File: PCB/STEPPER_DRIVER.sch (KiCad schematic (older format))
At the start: 7 parts, among them J3 Screw_Terminal_01x04, J4 Conn_01x04_Female

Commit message: Added Dielectric and voltage rating to all capacitors
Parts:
- C10, C9: Dielectric (none) -> X7R
- C11: Dielectric (none) -> Tantalum
- C12: Dielectric (none) -> Aluminium Film; Impedance (none) -> General Purpose; Lifetime @ Temperature (none) -> 1000hr @ 85degC
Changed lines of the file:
@@
 $Descr A4 11693 8268
 encoding utf-8
-Sheet 3 20
+Sheet 13 20
 Title ""
 Date ""
@@
 F 3 "" H 5950 2500 50  0001 C CNN
 F 4 "50V" H 5950 2500 50  0001 C CNN "Voltage Rating"
+F 5 "Tantalum" H 5950 2500 50  0001 C CNN "Dielectric"
 	1    5950 2500
 	1    0    0    -1
@@
 F 3 "" H 5600 2500 50  0001 C CNN
 F 4 "50V" H 5600 2500 50  0001 C CNN "Voltage Rating"
+F 5 "X7R" H 5600 2500 50  0001 C CNN "Dielectric"
 	1    5600 2500
 	1    0    0    -1
@@
 F 3 "" H 6350 2500 50  0001 C CNN
 F 4 "50V" H 6350 2500 50  0001 C CNN "Voltage Rating"
+F 5 "Aluminium Film" H 6350 2500 50  0001 C CNN "Dielectric"
+F 6 "General Purpose" H 6350 2500 50  0001 C CNN "Impedance"
+F 7 "1000hr @ 85degC" H 6350 2500 50  0001 C CNN "Lifetime @ Temperature"
 	1    6350 2500
 	1    0    0    -1
@@
 F 3 "" H 5250 2500 50  0001 C CNN
 F 4 "6.3V" H 5250 2500 50  0001 C CNN "Voltage Rating"
+F 5 "X7R" H 5250 2500 50  0001 C CNN "Dielectric"
 	1    5250 2500
 	1    0    0    -1

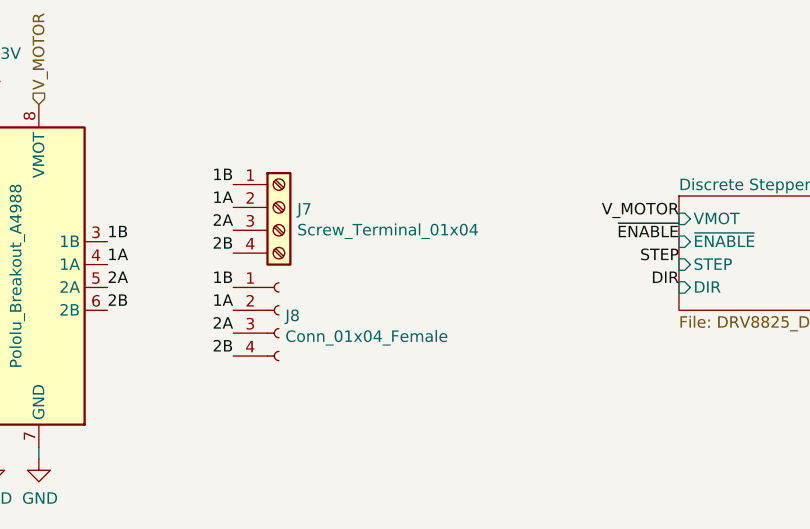
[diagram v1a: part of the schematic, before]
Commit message: Named elements with missing values
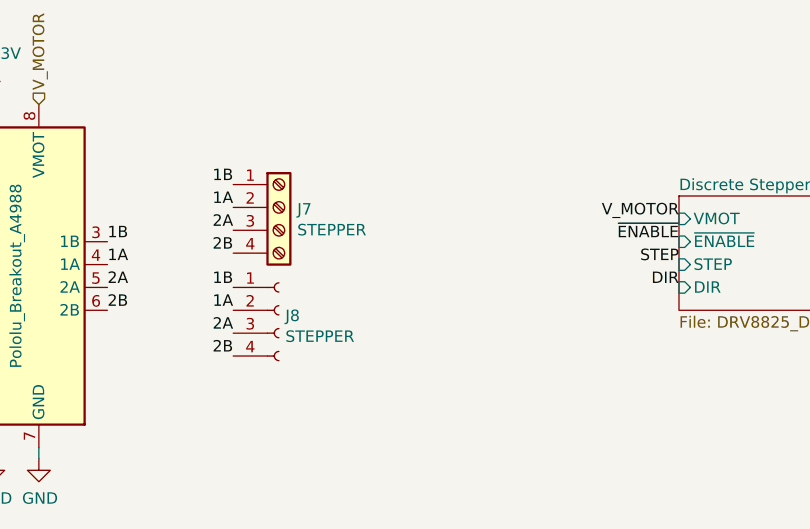
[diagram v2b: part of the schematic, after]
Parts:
- J3: value Screw_Terminal_01x04 -> STEPPER
- J4: value Conn_01x04_Female -> STEPPER
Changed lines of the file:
@@
 $Descr A4 11693 8268
 encoding utf-8
-Sheet 13 20
+Sheet 3 20
 Title ""
 Date ""
@@
 AR Path="/5E8813FF/5E8A7820" Ref="J8"  Part="1"
 F 0 "J8" H 6978 4226 50  0000 L CNN
-F 1 "Conn_01x04_Female" H 6978 4135 50  0000 L CNN
+F 1 "STEPPER" H 6978 4135 50  0000 L CNN
 F 2 "" H 6950 4250 50  0001 C CNN
 F 3 "" H 6950 4250 50  0001 C CNN
@@
 AR Path="/5E8813FF/5E8A82D9" Ref="J7"  Part="1"
 F 0 "J7" H 7030 3792 50  0000 L CNN
-F 1 "Screw_Terminal_01x04" H 7030 3701 50  0000 L CNN
+F 1 "STEPPER" H 7030 3701 50  0000 L CNN
 F 2 "" H 6950 3800 50  0001 C CNN
 F 3 "" H 6950 3800 50  0001 C CNN
@@
 AR Path="/5E8A6686/5E8421AB" Ref="#PWR033"  Part="1"
 AR Path="/5E8813FF/5E8421AB" Ref="#PWR096"  Part="1"
-F 0 "#PWR096" H 5700 3150 50  0001 C CNN
+F 0 "#PWR033" H 5700 3150 50  0001 C CNN
 F 1 "+3.3V" H 5715 3473 50  0000 C CNN
 F 2 "" H 5700 3300 50  0001 C CNN
@@
 AR Path="/5E8A6686/5E842853" Ref="#PWR034"  Part="1"
 AR Path="/5E8813FF/5E842853" Ref="#PWR097"  Part="1"
-F 0 "#PWR097" H 5700 4650 50  0001 C CNN
+F 0 "#PWR034" H 5700 4650 50  0001 C CNN
 F 1 "GND" H 5705 4727 50  0000 C CNN
 F 2 "" H 5700 4900 50  0001 C CNN
@@
 AR Path="/5E8A6686/5E842AD6" Ref="#PWR035"  Part="1"
 AR Path="/5E8813FF/5E842AD6" Ref="#PWR098"  Part="1"
-F 0 "#PWR098" H 5900 4650 50  0001 C CNN
+F 0 "#PWR035" H 5900 4650 50  0001 C CNN
 F 1 "GND" H 5905 4727 50  0000 C CNN
 F 2 "" H 5900 4900 50  0001 C CNN
@@
 AR Path="/5E8A6686/5E84D212" Ref="#PWR027"  Part="1"
 AR Path="/5E8813FF/5E84D212" Ref="#PWR090"  Part="1"
-F 0 "#PWR090" H 5250 3400 50  0001 C CNN
+F 0 "#PWR027" H 5250 3400 50  0001 C CNN
 F 1 "GND" V 5255 3522 50  0000 R CNN
 F 2 "" H 5250 3650 50  0001 C CNN
@@
 AR Path="/5E8A6686/5E8548E7" Ref="#PWR036"  Part="1"
 AR Path="/5E8813FF/5E8548E7" Ref="#PWR099"  Part="1"
-F 0 "#PWR099" H 5950 2400 50  0001 C CNN
+F 0 "#PWR036" H 5950 2400 50  0001 C CNN
 F 1 "GND" H 5955 2477 50  0000 C CNN
 F 2 "" H 5950 2650 50  0001 C CNN
@@
 AR Path="/5E8A6686/5E8572FE" Ref="#PWR032"  Part="1"
 AR Path="/5E8813FF/5E8572FE" Ref="#PWR095"  Part="1"
-F 0 "#PWR095" H 5600 2400 50  0001 C CNN
+F 0 "#PWR032" H 5600 2400 50  0001 C CNN
 F 1 "GND" H 5605 2477 50  0000 C CNN
 F 2 "" H 5600 2650 50  0001 C CNN
@@
 AR Path="/5E8A6686/5E85775C" Ref="#PWR037"  Part="1"
 AR Path="/5E8813FF/5E85775C" Ref="#PWR0100"  Part="1"
-F 0 "#PWR0100" H 6350 2400 50  0001 C CNN
+F 0 "#PWR037" H 6350 2400 50  0001 C CNN
 F 1 "GND" H 6355 2477 50  0000 C CNN
 F 2 "" H 6350 2650 50  0001 C CNN
@@
 AR Path="/5E8A6686/5E860428" Ref="#PWR026"  Part="1"
 AR Path="/5E8813FF/5E860428" Ref="#PWR089"  Part="1"
-F 0 "#PWR089" H 5250 2400 50  0001 C CNN
+F 0 "#PWR026" H 5250 2400 50  0001 C CNN
 F 1 "GND" H 5255 2477 50  0000 C CNN
 F 2 "" H 5250 2650 50  0001 C CNN
@@
 AR Path="/5E8A6686/5E8608E5" Ref="#PWR025"  Part="1"
 AR Path="/5E8813FF/5E8608E5" Ref="#PWR088"  Part="1"
-F 0 "#PWR088" H 5250 2200 50  0001 C CNN
+F 0 "#PWR025" H 5250 2200 50  0001 C CNN
 F 1 "+3.3V" H 5265 2523 50  0000 C CNN
 F 2 "" H 5250 2350 50  0001 C CNN
@@
 AR Path="/5E8A6686/5E8CF9B2" Ref="#PWR028"  Part="1"
 AR Path="/5E8813FF/5E8CF9B2" Ref="#PWR091"  Part="1"
-F 0 "#PWR091" H 5250 3500 50  0001 C CNN
+F 0 "#PWR028" H 5250 3500 50  0001 C CNN
 F 1 "GND" V 5255 3622 50  0000 R CNN
 F 2 "" H 5250 3750 50  0001 C CNN
@@
 AR Path="/5E8A6686/5E8FF25B" Ref="#PWR029"  Part="1"
 AR Path="/5E8813FF/5E8FF25B" Ref="#PWR092"  Part="1"
-F 0 "#PWR092" H 5250 4100 50  0001 C CNN
+F 0 "#PWR029" H 5250 4100 50  0001 C CNN
 F 1 "GND" V 5255 4222 50  0000 R CNN
 F 2 "" H 5250 4350 50  0001 C CNN
@@
 AR Path="/5E8A6686/5E8FF51C" Ref="#PWR030"  Part="1"
 AR Path="/5E8813FF/5E8FF51C" Ref="#PWR093"  Part="1"
-F 0 "#PWR093" H 5250 4200 50  0001 C CNN
+F 0 "#PWR030" H 5250 4200 50  0001 C CNN
 F 1 "GND" V 5255 4322 50  0000 R CNN
 F 2 "" H 5250 4450 50  0001 C CNN
@@
 AR Path="/5E8A6686/5E8FF61C" Ref="#PWR031"  Part="1"
 AR Path="/5E8813FF/5E8FF61C" Ref="#PWR094"  Part="1"
-F 0 "#PWR094" H 5250 4300 50  0001 C CNN
+F 0 "#PWR031" H 5250 4300 50  0001 C CNN
 F 1 "GND" V 5255 4422 50  0000 R CNN
 F 2 "" H 5250 4550 50  0001 C CNN

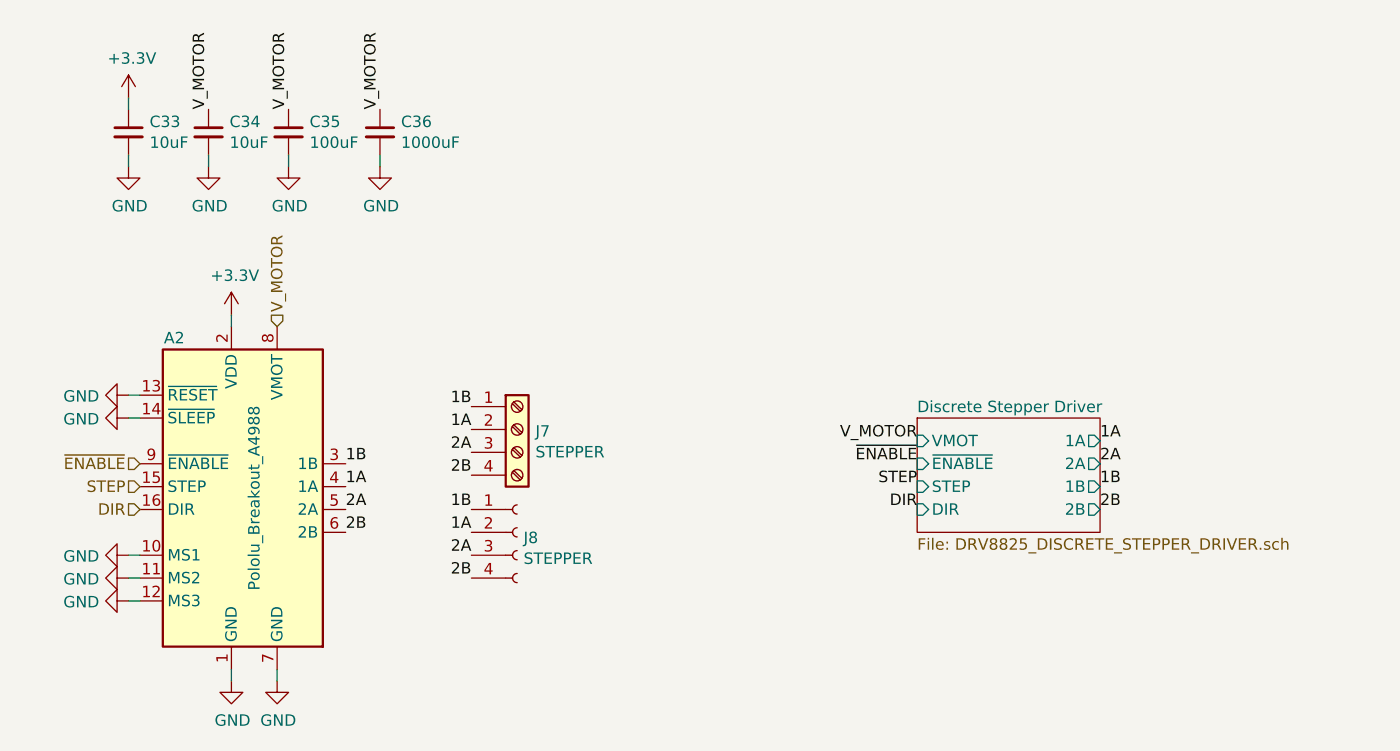
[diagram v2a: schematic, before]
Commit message: Added some footprints
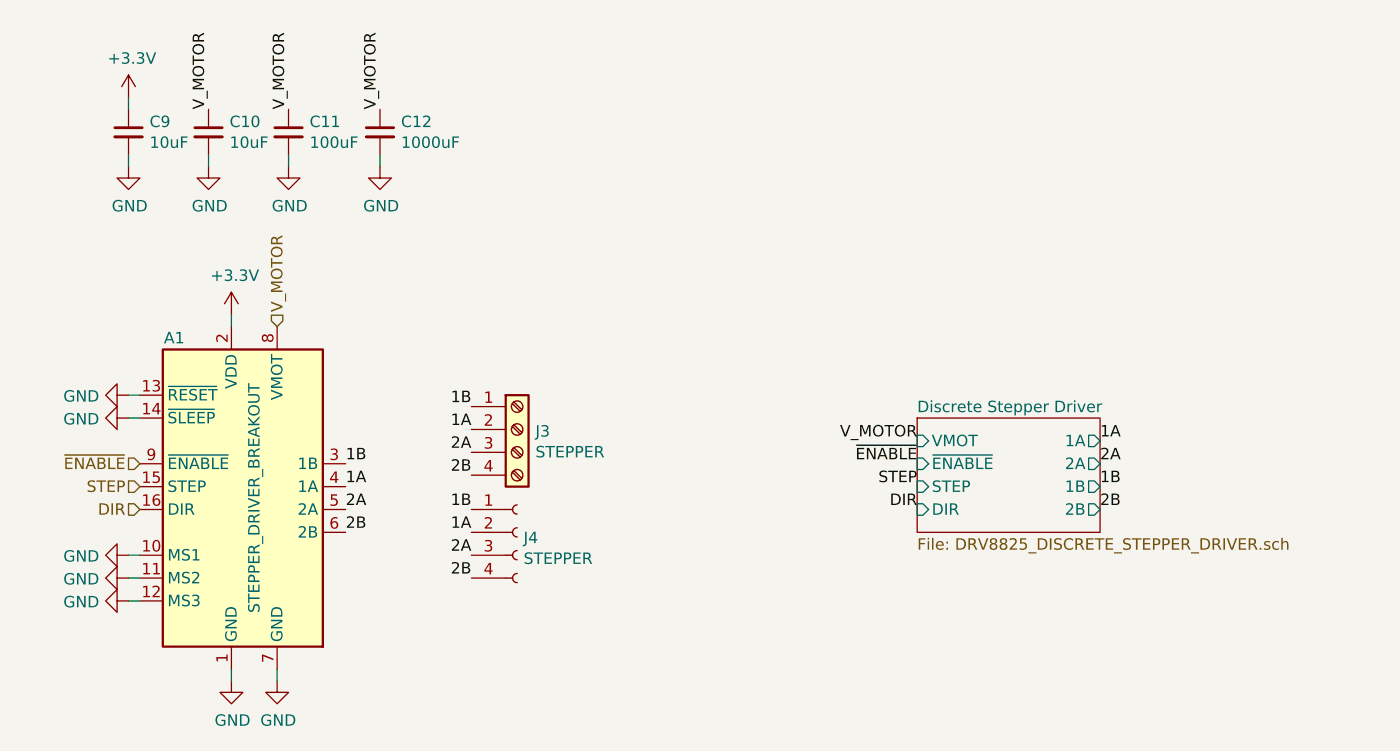
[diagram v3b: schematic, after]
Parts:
- A1: value Pololu_Breakout_A4988 -> STEPPER_DRIVER_BREAKOUT
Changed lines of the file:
@@
 AR Path="/5E8A6686/5E8A6F90" Ref="A1"  Part="1"
 AR Path="/5E8813FF/5E8A6F90" Ref="A2"  Part="1"
-F 0 "A2" H 5450 4700 50  0000 C CNN
-F 1 "Pololu_Breakout_A4988" V 5800 4000 50  0000 C CNN
+F 0 "A1" H 5450 4700 50  0000 C CNN
+F 1 "STEPPER_DRIVER_BREAKOUT" V 5800 4000 50  0000 C CNN
 F 2 "Module:Pololu_Breakout-16_15.2x20.3mm" H 5975 3300 50  0001 L CNN
 F 3 "https://www.pololu.com/product/2980/pictures" H 5800 3750 50  0001 C CNN
@@
 AR Path="/5E8A6686/5E8A7820" Ref="J4"  Part="1"
 AR Path="/5E8813FF/5E8A7820" Ref="J8"  Part="1"
-F 0 "J8" H 6978 4226 50  0000 L CNN
+F 0 "J4" H 6978 4226 50  0000 L CNN
 F 1 "STEPPER" H 6978 4135 50  0000 L CNN
 F 2 "" H 6950 4250 50  0001 C CNN
@@
 AR Path="/5E8A6686/5E8A82D9" Ref="J3"  Part="1"
 AR Path="/5E8813FF/5E8A82D9" Ref="J7"  Part="1"
-F 0 "J7" H 7030 3792 50  0000 L CNN
+F 0 "J3" H 7030 3792 50  0000 L CNN
 F 1 "STEPPER" H 7030 3701 50  0000 L CNN
 F 2 "" H 6950 3800 50  0001 C CNN
@@
 AR Path="/5E8A6686/5E8548E0" Ref="C11"  Part="1"
 AR Path="/5E8813FF/5E8548E0" Ref="C35"  Part="1"
-F 0 "C35" H 6042 2546 50  0000 L CNN
+F 0 "C11" H 6042 2546 50  0000 L CNN
 F 1 "100uF" H 6042 2455 50  0000 L CNN
 F 2 "" H 5950 2500 50  0001 C CNN
@@
 AR Path="/5E8A6686/5E8572F7" Ref="C10"  Part="1"
 AR Path="/5E8813FF/5E8572F7" Ref="C34"  Part="1"
-F 0 "C34" H 5692 2546 50  0000 L CNN
+F 0 "C10" H 5692 2546 50  0000 L CNN
 F 1 "10uF" H 5692 2455 50  0000 L CNN
 F 2 "" H 5600 2500 50  0001 C CNN
@@
 AR Path="/5E8A6686/5E857755" Ref="C12"  Part="1"
 AR Path="/5E8813FF/5E857755" Ref="C36"  Part="1"
-F 0 "C36" H 6442 2546 50  0000 L CNN
+F 0 "C12" H 6442 2546 50  0000 L CNN
 F 1 "1000uF" H 6442 2455 50  0000 L CNN
 F 2 "" H 6350 2500 50  0001 C CNN
@@
 AR Path="/5E8A6686/5E860421" Ref="C9"  Part="1"
 AR Path="/5E8813FF/5E860421" Ref="C33"  Part="1"
-F 0 "C33" H 5342 2546 50  0000 L CNN
+F 0 "C9" H 5342 2546 50  0000 L CNN
 F 1 "10uF" H 5342 2455 50  0000 L CNN
 F 2 "" H 5250 2500 50  0001 C CNN

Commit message: Added optical linear encoder
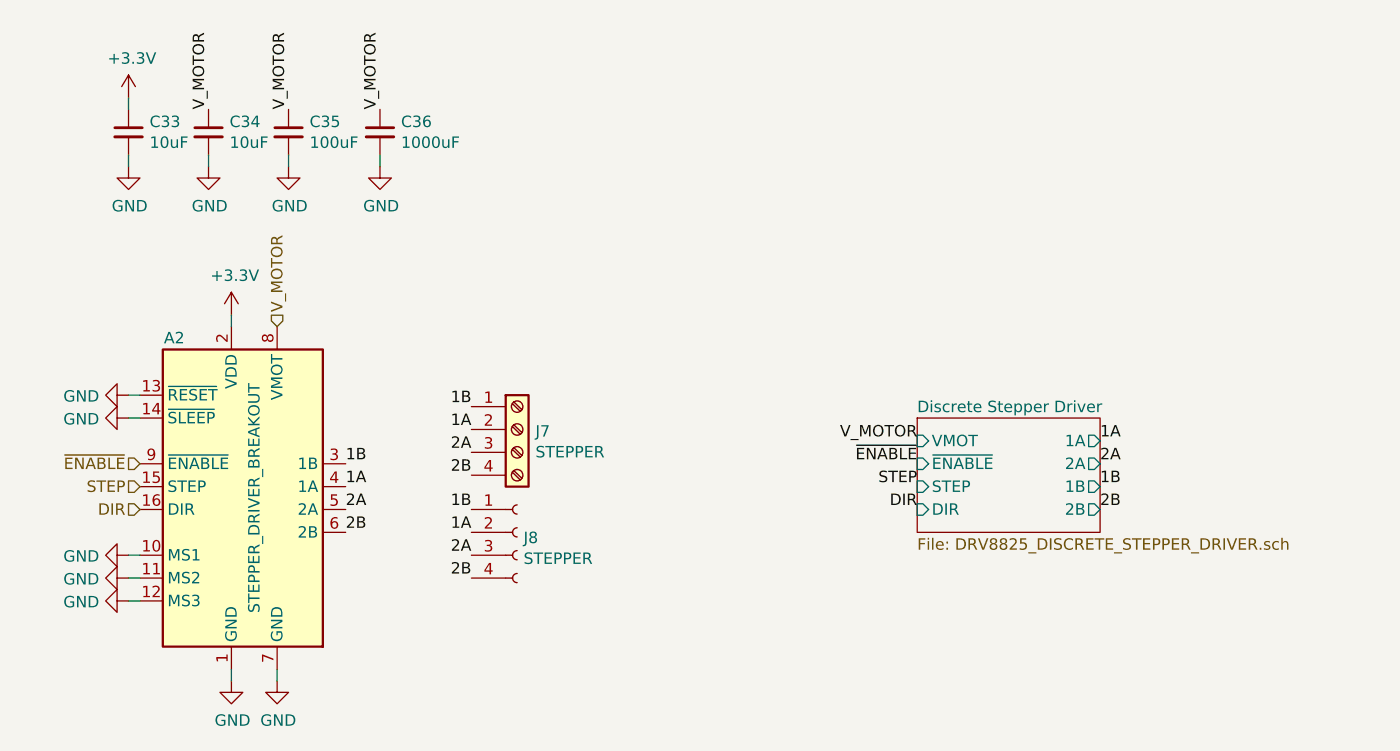
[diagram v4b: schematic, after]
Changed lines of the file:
@@
 $Descr A4 11693 8268
 encoding utf-8
-Sheet 3 20
+Sheet 3 21
 Title ""
 Date ""
@@
 AR Path="/5E8A6686/5E8A6F90" Ref="A1"  Part="1"
 AR Path="/5E8813FF/5E8A6F90" Ref="A2"  Part="1"
-F 0 "A1" H 5450 4700 50  0000 C CNN
+F 0 "A2" H 5450 4700 50  0000 C CNN
 F 1 "STEPPER_DRIVER_BREAKOUT" V 5800 4000 50  0000 C CNN
 F 2 "Module:Pololu_Breakout-16_15.2x20.3mm" H 5975 3300 50  0001 L CNN
@@
 AR Path="/5E8A6686/5E8A7820" Ref="J4"  Part="1"
 AR Path="/5E8813FF/5E8A7820" Ref="J8"  Part="1"
-F 0 "J4" H 6978 4226 50  0000 L CNN
+F 0 "J8" H 6978 4226 50  0000 L CNN
 F 1 "STEPPER" H 6978 4135 50  0000 L CNN
 F 2 "" H 6950 4250 50  0001 C CNN
@@
 AR Path="/5E8A6686/5E8A82D9" Ref="J3"  Part="1"
 AR Path="/5E8813FF/5E8A82D9" Ref="J7"  Part="1"
-F 0 "J3" H 7030 3792 50  0000 L CNN
+F 0 "J7" H 7030 3792 50  0000 L CNN
 F 1 "STEPPER" H 7030 3701 50  0000 L CNN
 F 2 "" H 6950 3800 50  0001 C CNN
@@
 AR Path="/5E8A6686/5E8421AB" Ref="#PWR033"  Part="1"
 AR Path="/5E8813FF/5E8421AB" Ref="#PWR096"  Part="1"
-F 0 "#PWR033" H 5700 3150 50  0001 C CNN
+F 0 "#PWR096" H 5700 3150 50  0001 C CNN
 F 1 "+3.3V" H 5715 3473 50  0000 C CNN
 F 2 "" H 5700 3300 50  0001 C CNN
@@
 AR Path="/5E8A6686/5E842853" Ref="#PWR034"  Part="1"
 AR Path="/5E8813FF/5E842853" Ref="#PWR097"  Part="1"
-F 0 "#PWR034" H 5700 4650 50  0001 C CNN
+F 0 "#PWR097" H 5700 4650 50  0001 C CNN
 F 1 "GND" H 5705 4727 50  0000 C CNN
 F 2 "" H 5700 4900 50  0001 C CNN
@@
 AR Path="/5E8A6686/5E842AD6" Ref="#PWR035"  Part="1"
 AR Path="/5E8813FF/5E842AD6" Ref="#PWR098"  Part="1"
-F 0 "#PWR035" H 5900 4650 50  0001 C CNN
+F 0 "#PWR098" H 5900 4650 50  0001 C CNN
 F 1 "GND" H 5905 4727 50  0000 C CNN
 F 2 "" H 5900 4900 50  0001 C CNN
@@
 AR Path="/5E8A6686/5E84D212" Ref="#PWR027"  Part="1"
 AR Path="/5E8813FF/5E84D212" Ref="#PWR090"  Part="1"
-F 0 "#PWR027" H 5250 3400 50  0001 C CNN
+F 0 "#PWR090" H 5250 3400 50  0001 C CNN
 F 1 "GND" V 5255 3522 50  0000 R CNN
 F 2 "" H 5250 3650 50  0001 C CNN
@@
 AR Path="/5E8A6686/5E8548E0" Ref="C11"  Part="1"
 AR Path="/5E8813FF/5E8548E0" Ref="C35"  Part="1"
-F 0 "C11" H 6042 2546 50  0000 L CNN
+F 0 "C35" H 6042 2546 50  0000 L CNN
 F 1 "100uF" H 6042 2455 50  0000 L CNN
 F 2 "" H 5950 2500 50  0001 C CNN
@@
 AR Path="/5E8A6686/5E8548E7" Ref="#PWR036"  Part="1"
 AR Path="/5E8813FF/5E8548E7" Ref="#PWR099"  Part="1"
-F 0 "#PWR036" H 5950 2400 50  0001 C CNN
+F 0 "#PWR099" H 5950 2400 50  0001 C CNN
 F 1 "GND" H 5955 2477 50  0000 C CNN
 F 2 "" H 5950 2650 50  0001 C CNN
@@
 AR Path="/5E8A6686/5E8572F7" Ref="C10"  Part="1"
 AR Path="/5E8813FF/5E8572F7" Ref="C34"  Part="1"
-F 0 "C10" H 5692 2546 50  0000 L CNN
+F 0 "C34" H 5692 2546 50  0000 L CNN
 F 1 "10uF" H 5692 2455 50  0000 L CNN
 F 2 "" H 5600 2500 50  0001 C CNN
@@
 AR Path="/5E8A6686/5E8572FE" Ref="#PWR032"  Part="1"
 AR Path="/5E8813FF/5E8572FE" Ref="#PWR095"  Part="1"
-F 0 "#PWR032" H 5600 2400 50  0001 C CNN
+F 0 "#PWR095" H 5600 2400 50  0001 C CNN
 F 1 "GND" H 5605 2477 50  0000 C CNN
 F 2 "" H 5600 2650 50  0001 C CNN
@@
 AR Path="/5E8A6686/5E857755" Ref="C12"  Part="1"
 AR Path="/5E8813FF/5E857755" Ref="C36"  Part="1"
-F 0 "C12" H 6442 2546 50  0000 L CNN
+F 0 "C36" H 6442 2546 50  0000 L CNN
 F 1 "1000uF" H 6442 2455 50  0000 L CNN
 F 2 "" H 6350 2500 50  0001 C CNN
@@
 AR Path="/5E8A6686/5E85775C" Ref="#PWR037"  Part="1"
 AR Path="/5E8813FF/5E85775C" Ref="#PWR0100"  Part="1"
-F 0 "#PWR037" H 6350 2400 50  0001 C CNN
+F 0 "#PWR0100" H 6350 2400 50  0001 C CNN
 F 1 "GND" H 6355 2477 50  0000 C CNN
 F 2 "" H 6350 2650 50  0001 C CNN
@@
 AR Path="/5E8A6686/5E860421" Ref="C9"  Part="1"
 AR Path="/5E8813FF/5E860421" Ref="C33"  Part="1"
-F 0 "C9" H 5342 2546 50  0000 L CNN
+F 0 "C33" H 5342 2546 50  0000 L CNN
 F 1 "10uF" H 5342 2455 50  0000 L CNN
 F 2 "" H 5250 2500 50  0001 C CNN
@@
 AR Path="/5E8A6686/5E860428" Ref="#PWR026"  Part="1"
 AR Path="/5E8813FF/5E860428" Ref="#PWR089"  Part="1"
-F 0 "#PWR026" H 5250 2400 50  0001 C CNN
+F 0 "#PWR089" H 5250 2400 50  0001 C CNN
 F 1 "GND" H 5255 2477 50  0000 C CNN
 F 2 "" H 5250 2650 50  0001 C CNN
@@
 AR Path="/5E8A6686/5E8608E5" Ref="#PWR025"  Part="1"
 AR Path="/5E8813FF/5E8608E5" Ref="#PWR088"  Part="1"
-F 0 "#PWR025" H 5250 2200 50  0001 C CNN
+F 0 "#PWR088" H 5250 2200 50  0001 C CNN
 F 1 "+3.3V" H 5265 2523 50  0000 C CNN
 F 2 "" H 5250 2350 50  0001 C CNN
@@
 AR Path="/5E8A6686/5E8CF9B2" Ref="#PWR028"  Part="1"
 AR Path="/5E8813FF/5E8CF9B2" Ref="#PWR091"  Part="1"
-F 0 "#PWR028" H 5250 3500 50  0001 C CNN
+F 0 "#PWR091" H 5250 3500 50  0001 C CNN
 F 1 "GND" V 5255 3622 50  0000 R CNN
 F 2 "" H 5250 3750 50  0001 C CNN
@@
 AR Path="/5E8A6686/5E8FF25B" Ref="#PWR029"  Part="1"
 AR Path="/5E8813FF/5E8FF25B" Ref="#PWR092"  Part="1"
-F 0 "#PWR029" H 5250 4100 50  0001 C CNN
+F 0 "#PWR092" H 5250 4100 50  0001 C CNN
 F 1 "GND" V 5255 4222 50  0000 R CNN
 F 2 "" H 5250 4350 50  0001 C CNN
@@
 AR Path="/5E8A6686/5E8FF51C" Ref="#PWR030"  Part="1"
 AR Path="/5E8813FF/5E8FF51C" Ref="#PWR093"  Part="1"
-F 0 "#PWR030" H 5250 4200 50  0001 C CNN
+F 0 "#PWR093" H 5250 4200 50  0001 C CNN
 F 1 "GND" V 5255 4322 50  0000 R CNN
 F 2 "" H 5250 4450 50  0001 C CNN
@@
 AR Path="/5E8A6686/5E8FF61C" Ref="#PWR031"  Part="1"
 AR Path="/5E8813FF/5E8FF61C" Ref="#PWR094"  Part="1"
-F 0 "#PWR031" H 5250 4300 50  0001 C CNN
+F 0 "#PWR094" H 5250 4300 50  0001 C CNN
 F 1 "GND" V 5255 4422 50  0000 R CNN
 F 2 "" H 5250 4550 50  0001 C CNN
